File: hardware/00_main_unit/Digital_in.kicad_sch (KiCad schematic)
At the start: 52 parts

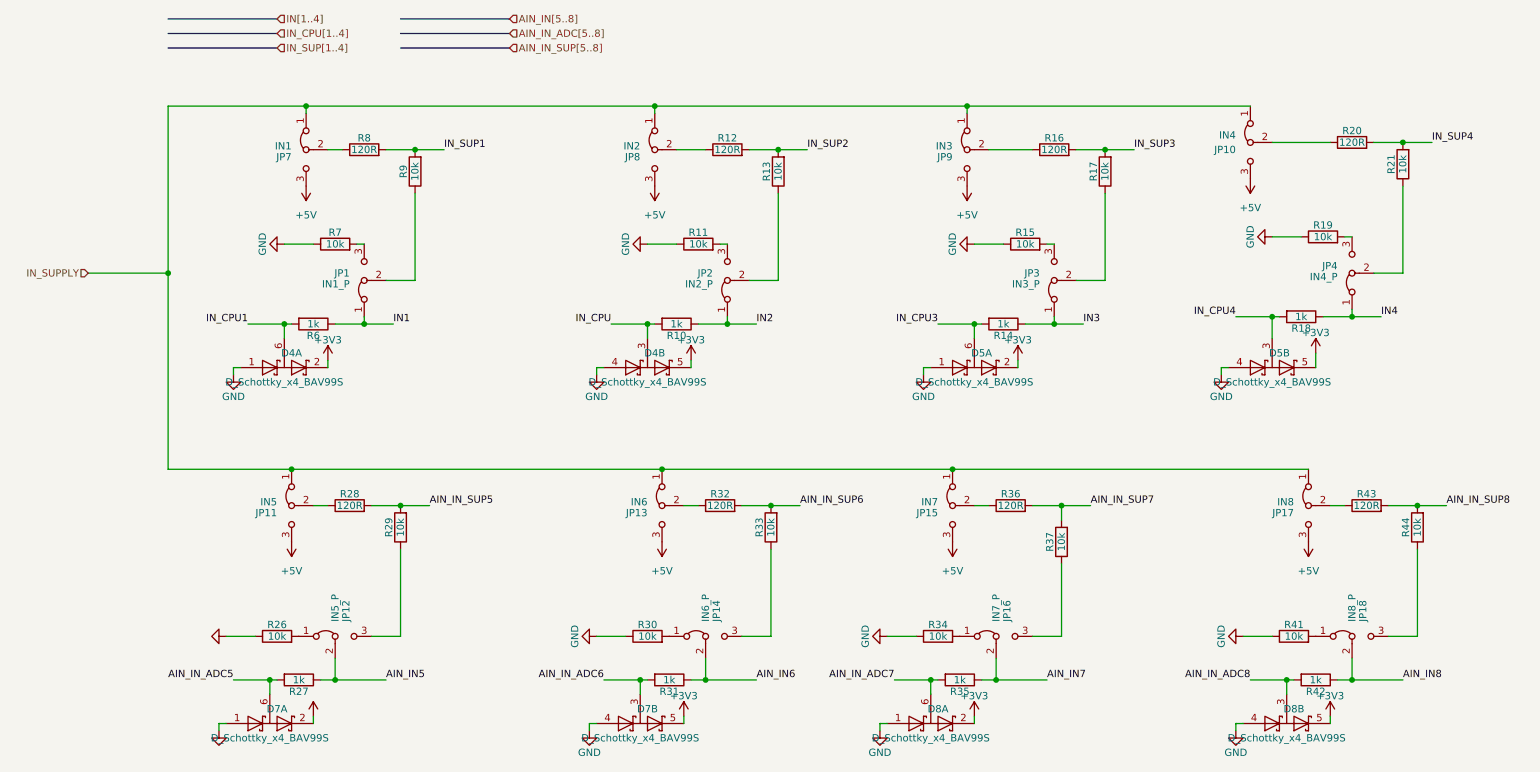
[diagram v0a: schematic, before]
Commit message: Fixes after wrong merge
Signed-off-by: Jacek <matuszewski.kartech@gmail.com>
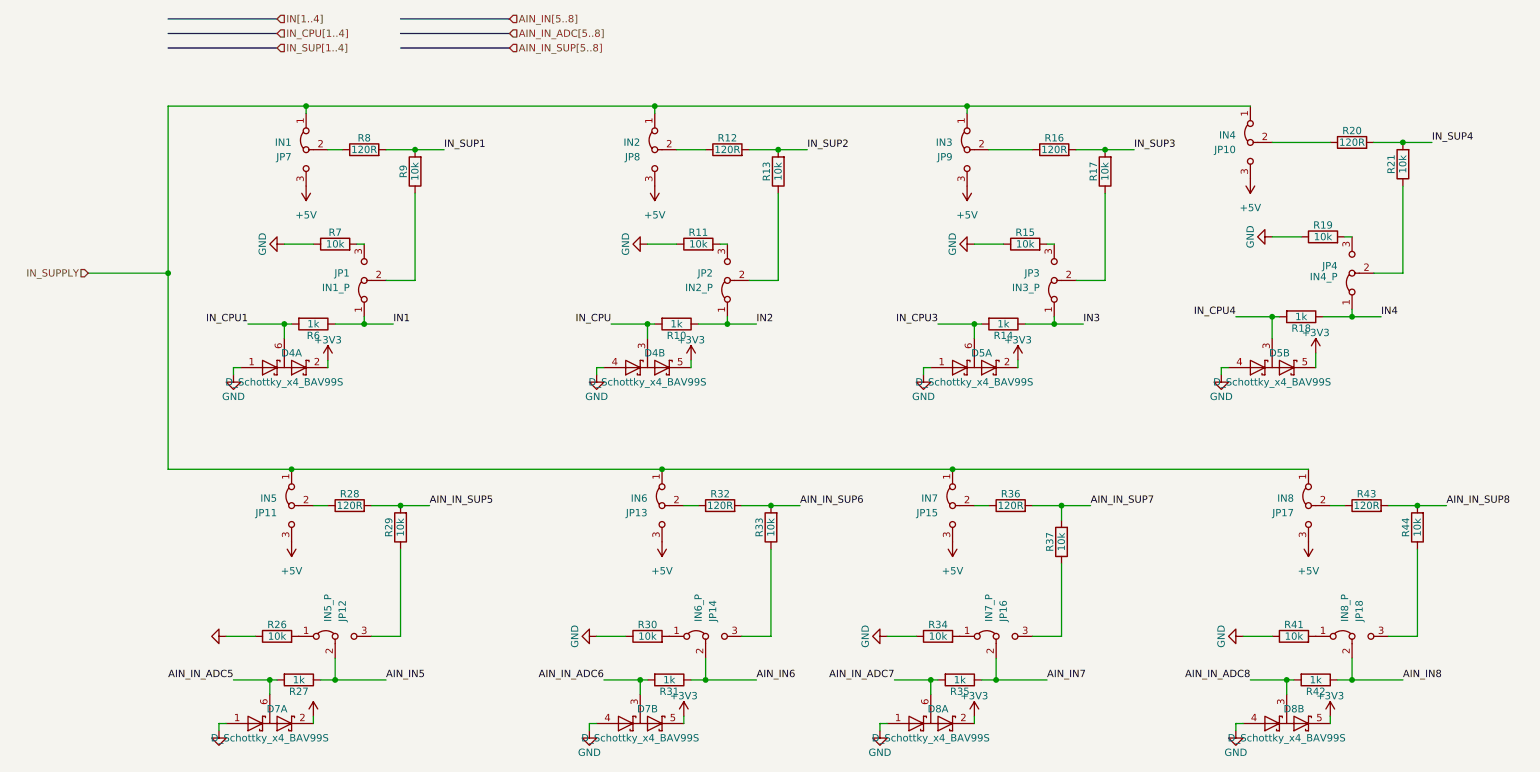
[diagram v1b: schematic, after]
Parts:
- R10, R14, R18, R27, R31, R35, R42, R6: TME SMD0603-1K -> (none)
- R11, R13, R15, R17, R19, R21, R26, R29, R30, R33, R34, R37, R41, R44, R7, R9: TME SMD0603-10K -> (none)
- R12, R16, R20, R28, R32, R36, R43, R8: TME WF06P-120R-5% -> (none)

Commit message: Fixes for new hw version
Signed-off-by: Jarosław Karwik <jaroslaw.karwik@gmail.com>
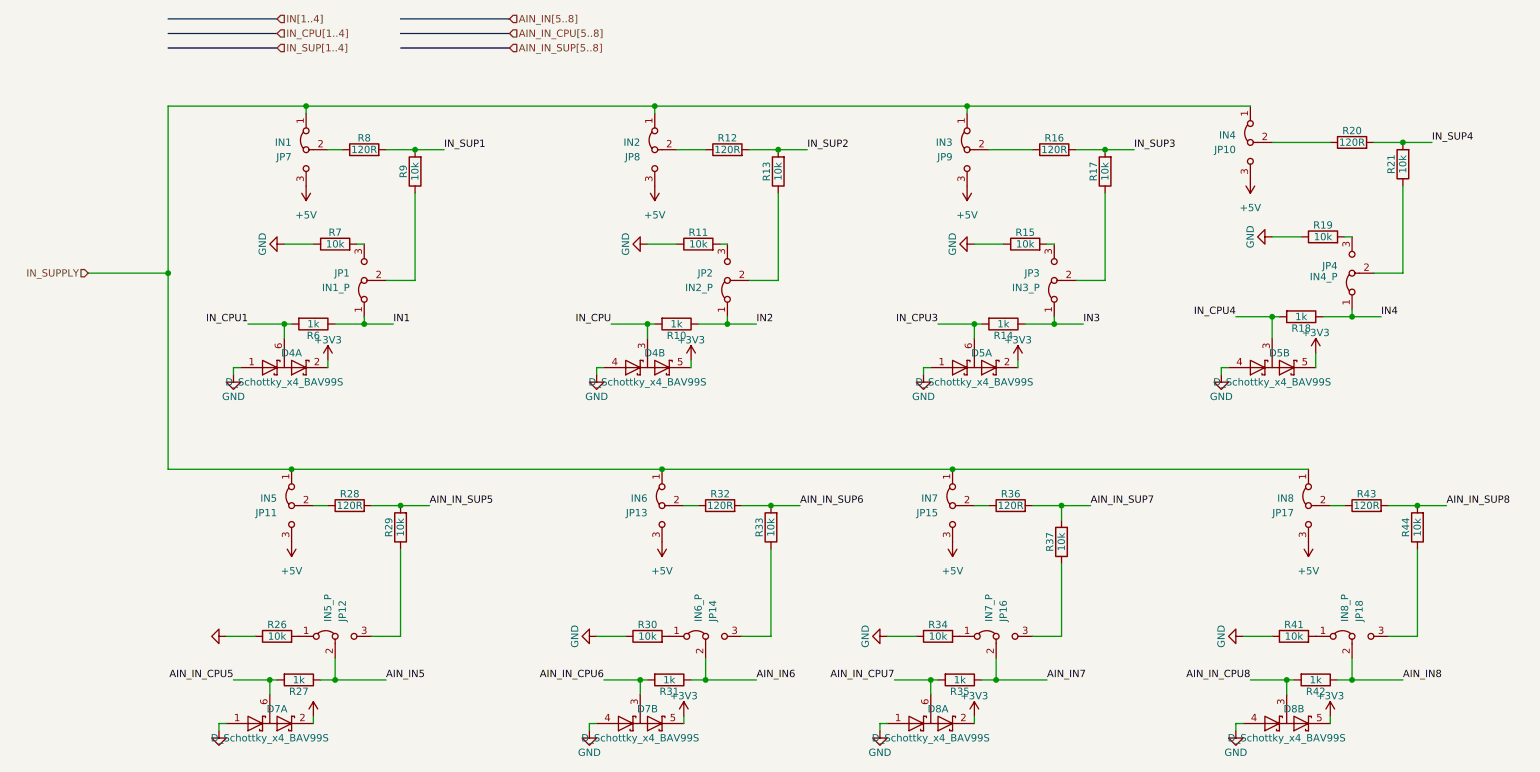
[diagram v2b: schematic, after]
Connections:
- net AIN_IN_ADC5 renamed AIN_IN_CPU5
- net AIN_IN_ADC6 renamed AIN_IN_CPU6
- net AIN_IN_ADC7 renamed AIN_IN_CPU7
- net AIN_IN_ADC8 renamed AIN_IN_CPU8
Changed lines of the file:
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@@
     (stroke (width 0) (type solid) (color 0 0 0 0))
   )
-  (label "AIN_IN_ADC5" (at 55.88 134.62 180)
+  (label "AIN_IN_CPU5" (at 55.88 134.62 180)
     (effects (font (size 1.27 1.27)) (justify right bottom))
   )
@@
     (effects (font (size 1.27 1.27)) (justify left bottom))
   )
-  (label "AIN_IN_ADC6" (at 120.65 134.62 180)
+  (label "AIN_IN_CPU6" (at 120.65 134.62 180)
     (effects (font (size 1.27 1.27)) (justify right bottom))
   )
@@
     (effects (font (size 1.27 1.27)) (justify left bottom))
   )
-  (label "AIN_IN_ADC7" (at 171.45 134.62 180)
+  (label "AIN_IN_CPU7" (at 171.45 134.62 180)
     (effects (font (size 1.27 1.27)) (justify right bottom))
   )
@@
     (effects (font (size 1.27 1.27)) (justify right bottom))
   )
-  (label "AIN_IN_ADC8" (at 233.68 134.62 180)
+  (label "AIN_IN_CPU8" (at 233.68 134.62 180)
     (effects (font (size 1.27 1.27)) (justify right bottom))
   )
@@
     (effects (font (size 1.27 1.27)) (justify left))
   )
-  (hierarchical_label "AIN_IN_ADC[5..8]" (shape input) (at 104.14 21.59 0)
+  (hierarchical_label "AIN_IN_CPU[5..8]" (shape input) (at 104.14 21.59 0)
     (effects (font (size 1.27 1.27)) (justify left))
   )

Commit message: Remote mode fixes
Signed-off-by: Jarosław Karwik <jaroslaw.karwik@gmail.com>
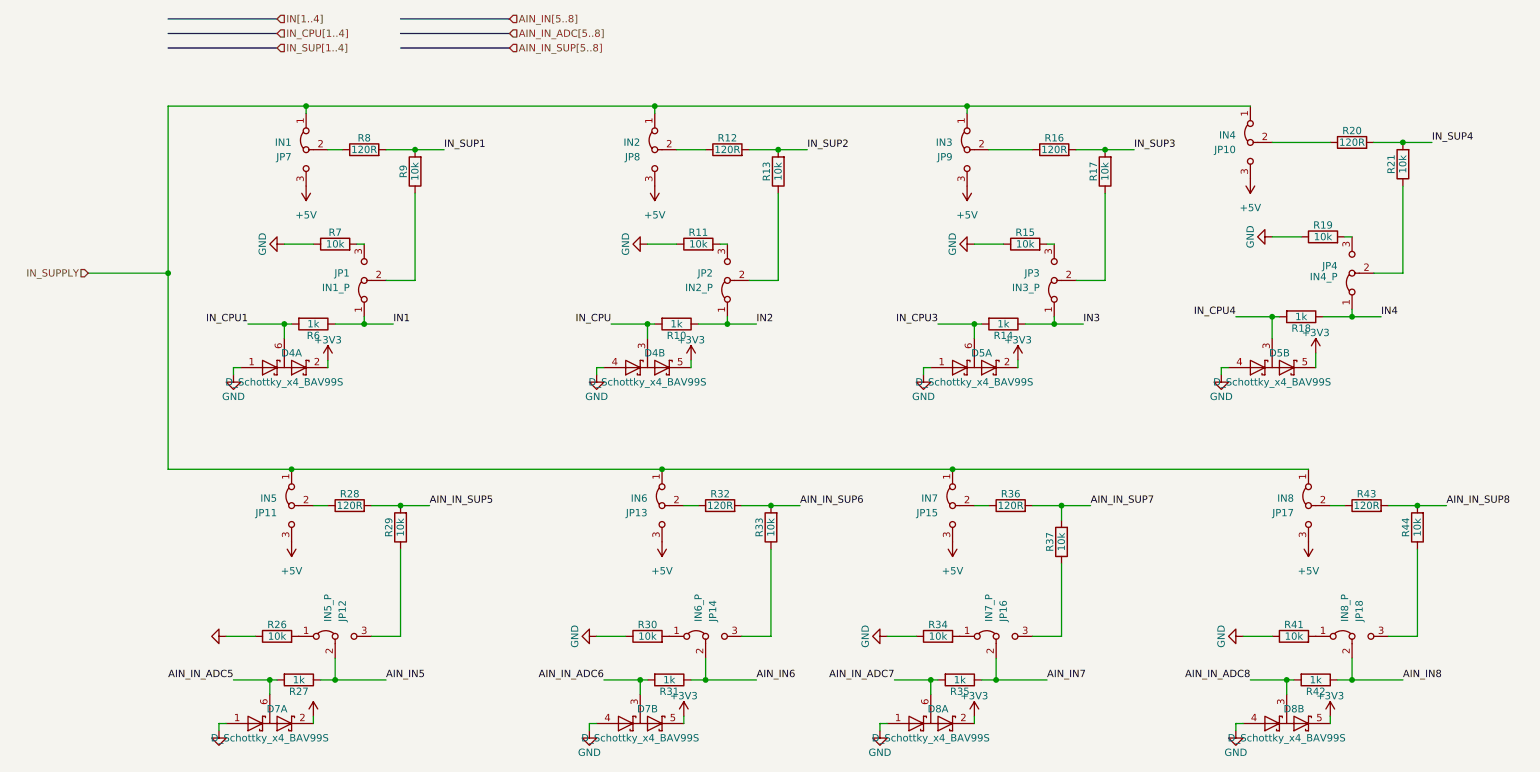
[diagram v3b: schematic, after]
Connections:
- net AIN_IN_CPU5 renamed AIN_IN_ADC5
- net AIN_IN_CPU6 renamed AIN_IN_ADC6
- net AIN_IN_CPU7 renamed AIN_IN_ADC7
- net AIN_IN_CPU8 renamed AIN_IN_ADC8
